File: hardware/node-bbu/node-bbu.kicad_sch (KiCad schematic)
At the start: 39 parts, among them J1 TERMINAL_BLK, J2 Conn_01x09_Pin, J3 Conn_01x02, J4 Conn_01x02, J5 Conn_01x09_Pin, J6 Conn_01x02, J7 Conn_01x02_Pin, J8 TERMINAL_BLK, J9 Conn_01x02_Socket, M1 Snubber_module_220VAC, M2 JQC-3FE-S-Z_MODULE, M3 TFT 1.8", M4 ZMCT103C, M5 ROTARY_ENC_W/SW_MODULE, M6 ADS1115, M7 ESP32-C3-ZERO, M8 4-24V to 5V buck, Q1 2N3904

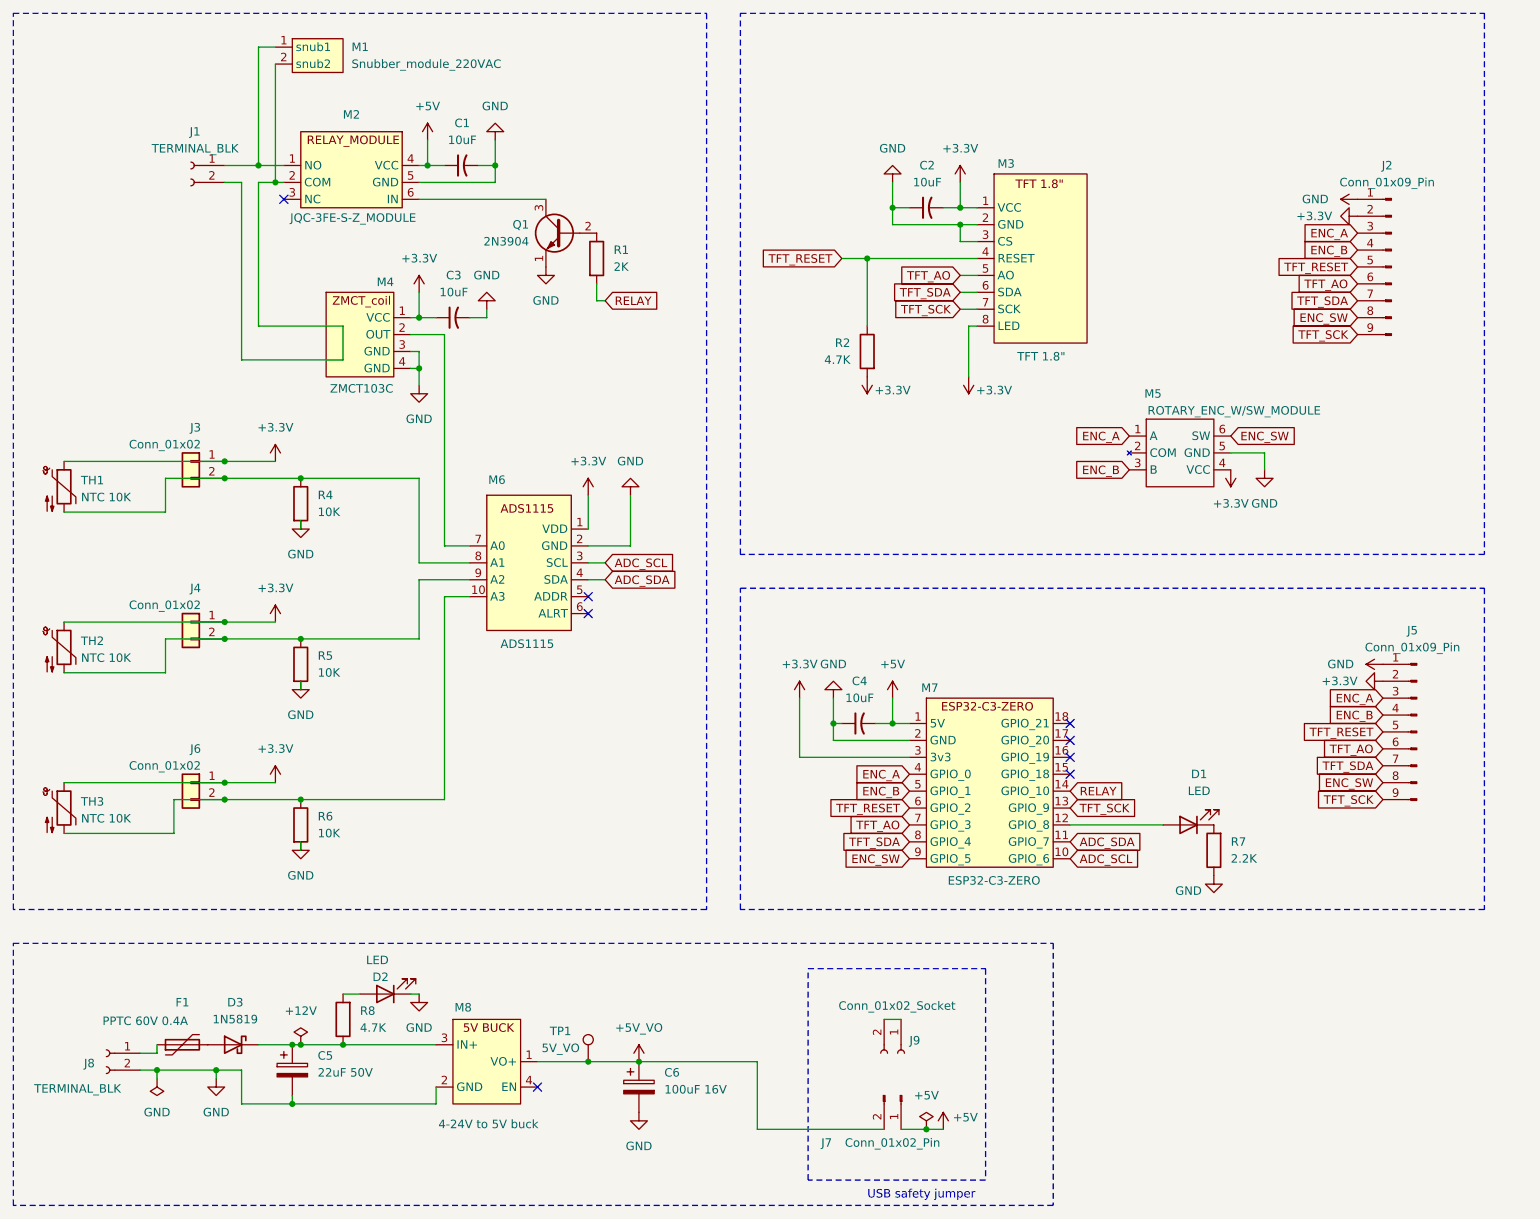
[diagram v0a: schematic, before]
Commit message: hardware: worktree reorg — bbu-controller split into node-bbu + gateway KiCad projects
- hardware/node-bbu/: v0.09 controller schematic/PCB as renamed from
  hardware/bbu-controller (same BOM/ERC/NETLIST exports)
- hardware/gateway/: gateway_protoype v0.01 project with BOM/ERC/NETLIST
- old hardware/bbu-controller/ tree removed (README + pin-mapping csv
  deleted; AGENTS.md pointer to the csv is now stale)
- .history/ and *.kicad_prl excluded via .gitignore

Schematics represent both protoboards now running in the field.
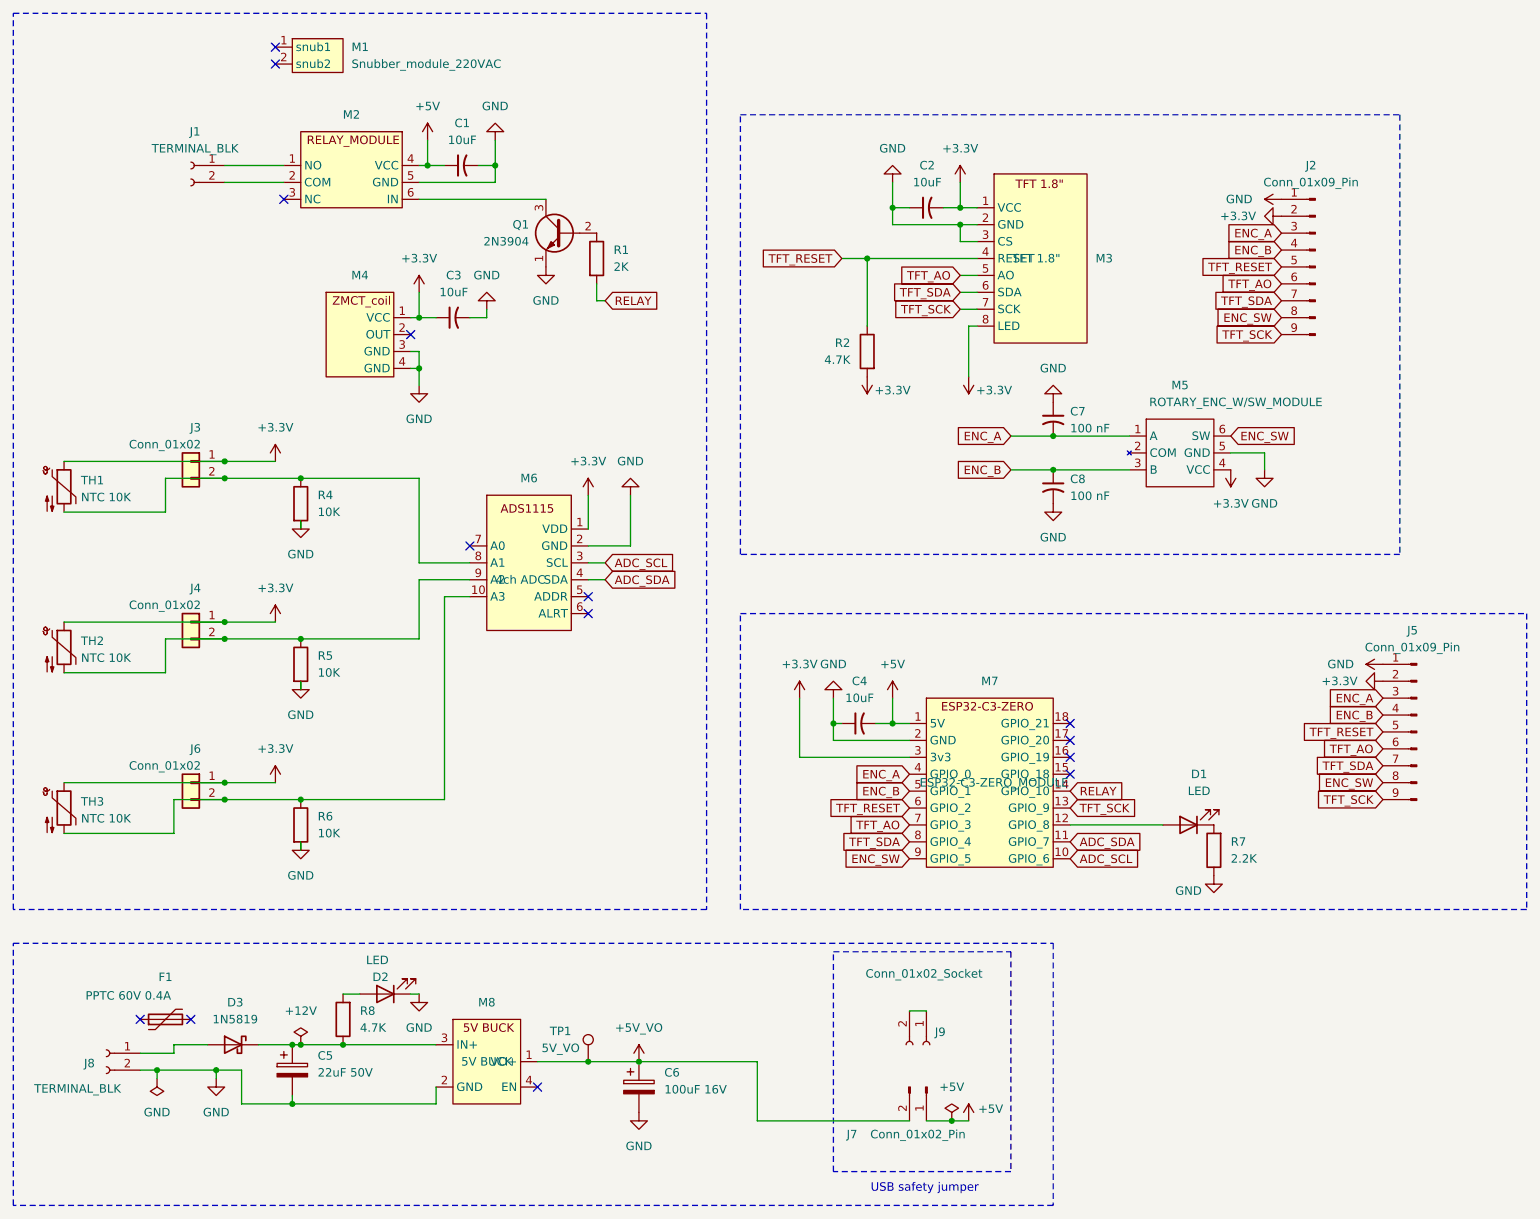
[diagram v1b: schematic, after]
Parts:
- removed M1: Snubber_module_220VAC, symbol 0_my_custom_library:SNUBBER_MODULE
- removed M2: JQC-3FE-S-Z_MODULE, symbol 0_my_custom_library:RELAY_MODULE
- removed M3: TFT 1.8", symbol 0_my_custom_library:1.8{dblquote}_TFT_MODULE
- removed M4: ZMCT103C, symbol 0_my_custom_library:ZMCT_COIL_MODULE
- removed M5: ROTARY_ENC_W/SW_MODULE, symbol 0_my_custom_library:ROTARY_ENC_W/SW_MODULE
- removed M6: ADS1115, symbol 0_my_custom_library:ADC_4CH_MODULE
- removed M7: ESP32-C3-ZERO, symbol 0_my_custom_library:ESP32-C3_ZERO_MODULE
- removed M8: 4-24V to 5V buck, symbol 0_my_custom_library:BUCK_6-24V_to_5V_MODULE
- added C7, C8: 100 nF, symbol Device:C_Small_US
- added M1: Snubber_module_220VAC, symbol 01_my_custom_library:SNUBBER_MODULE
- added M2: RELAY MODULE 5V SWITCH LOW, symbol 01_my_custom_library:RELAY_MODULE
- added M3: TFT 1.8", symbol 01_my_custom_library:1.8{dblquote}_TFT_MODULE
- added M4: (no value), symbol 01_my_custom_library:ZMCT_COIL_MODULE
- added M5: ROTARY_ENC_W/SW_MODULE, symbol 01_my_custom_library:ROTARY_ENC_W/SW_MODULE
- added M6: 4ch ADC, symbol 01_my_custom_library:ADC_4CH_MODULE
- added M7: ESP32-C3-ZERO_MODULE, symbol 01_my_custom_library:ESP32-C3_ZERO_MODULE
- added M8: 5V BUCK, symbol 01_my_custom_library:BUCK_6-24V_to_5V_MODULE
- F1: now left out of the parts list
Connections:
- net +3.3V: now also M3.1 (VCC), M3.8 (LED), M4.1 (VCC), M5.4 (VCC), M6.1 (VDD), M7.3 (3v3)
- net +5V: now also M2.4 (VCC), M7.1 (5V)
- net +5V_VO: now also M8.1 (VO+)
- net ADC_SCL: now also M6.3 (SCL), M7.10 (GPIO_6)
- net ADC_SDA: now also M6.4 (SDA), M7.11 (GPIO_7)
- net ENC_A: now also C7.2, M5.1 (A), M7.4 (GPIO_0)
- net ENC_B: now also C8.1, M5.3 (B), M7.5 (GPIO_1)
- net ENC_SW: now also M5.6 (SW), M7.9 (GPIO_5)
- net GND: now also C7.1, C8.2, M2.5 (GND), M3.2 (GND), M3.3 (CS), M4.3 (GND), M4.4 (GND), M5.5 (GND), M6.2 (GND), M7.2 (GND), M8.2 (GND)
- net RELAY: now also M7.14 (GPIO_10)
- net TFT_AO: now also M3.5 (AO), M7.7 (GPIO_3)
- net TFT_RESET: now also M3.4 (RESET), M7.6 (GPIO_2)
- net TFT_SCK: now also M3.7 (SCK), M7.13 (GPIO_9)
- net TFT_SDA: now also M3.6 (SDA), M7.8 (GPIO_4)
- net at J3.2 (Pin_2), R4.1, TH1.2: now also M6.8 (A1)
- net at C5.1, D3.1 (K), R8.1: now also M8.3 (IN+)
- net at D1.2 (A): now also M7.12 (GPIO_8)
- net at J1.1 (Pin_1): now also M2.1 (NO)
- net at J1.2 (Pin_2): now also M2.2 (COM)
- net at J6.2 (Pin_2), R6.1, TH3.2: now also M6.10 (A3)
- net at J8.1 (Pin_1): now also D3.2 (A); no longer F1.1
- net at J4.2 (Pin_2), R5.1, TH2.2: now also M6.9 (A2)
- net at F1.2: no longer D3.2 (A)
- net at Q1.3 (C): now also M2.6 (IN)
- no-connect marks 8 -> 14
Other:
- moved on the sheet: F1, J2, J7
